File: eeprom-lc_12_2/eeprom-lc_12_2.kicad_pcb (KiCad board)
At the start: 2 copper layers, 97 x 48.3 mm, 13 parts, among them J1 Screw_Terminal_01x03, U1 Controller-RP2040, U2 SN65176BD, U4 EEPROM-RP2040

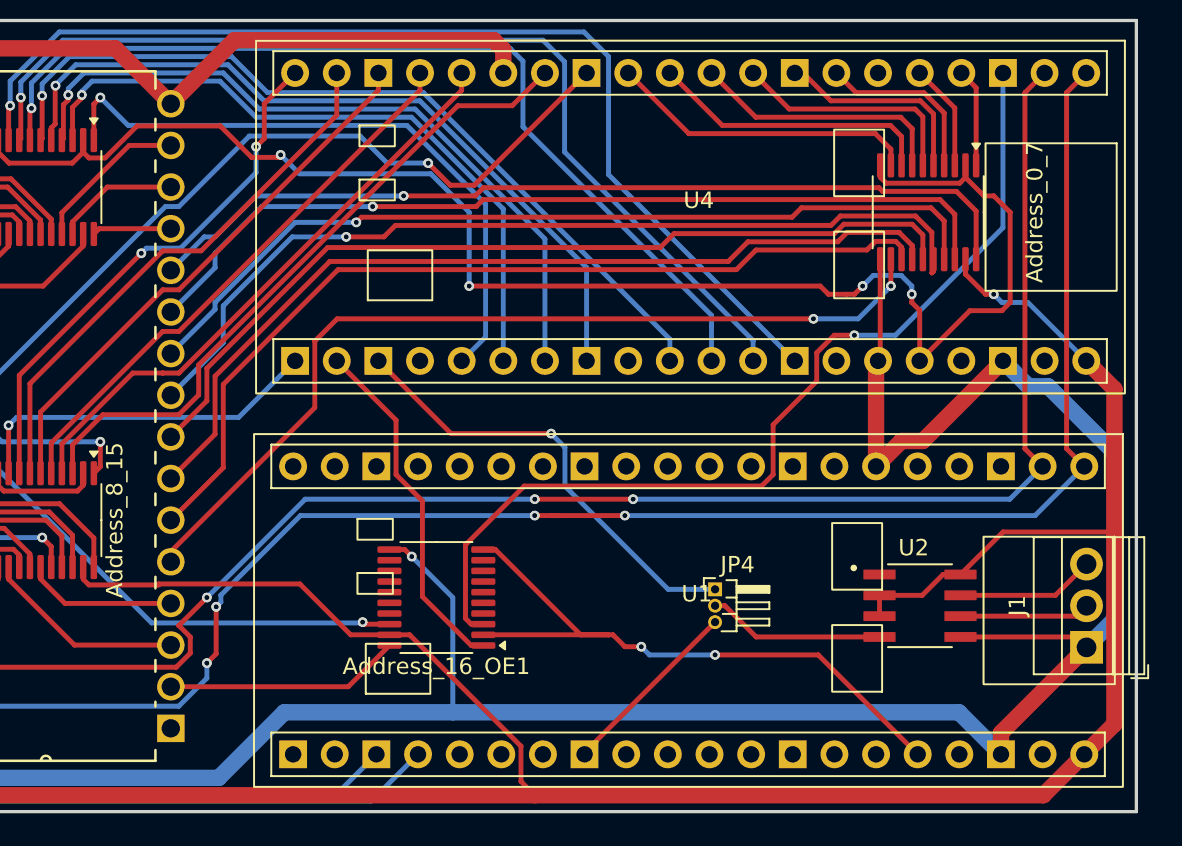
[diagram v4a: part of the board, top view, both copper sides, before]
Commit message: Fix wrong pinheaders
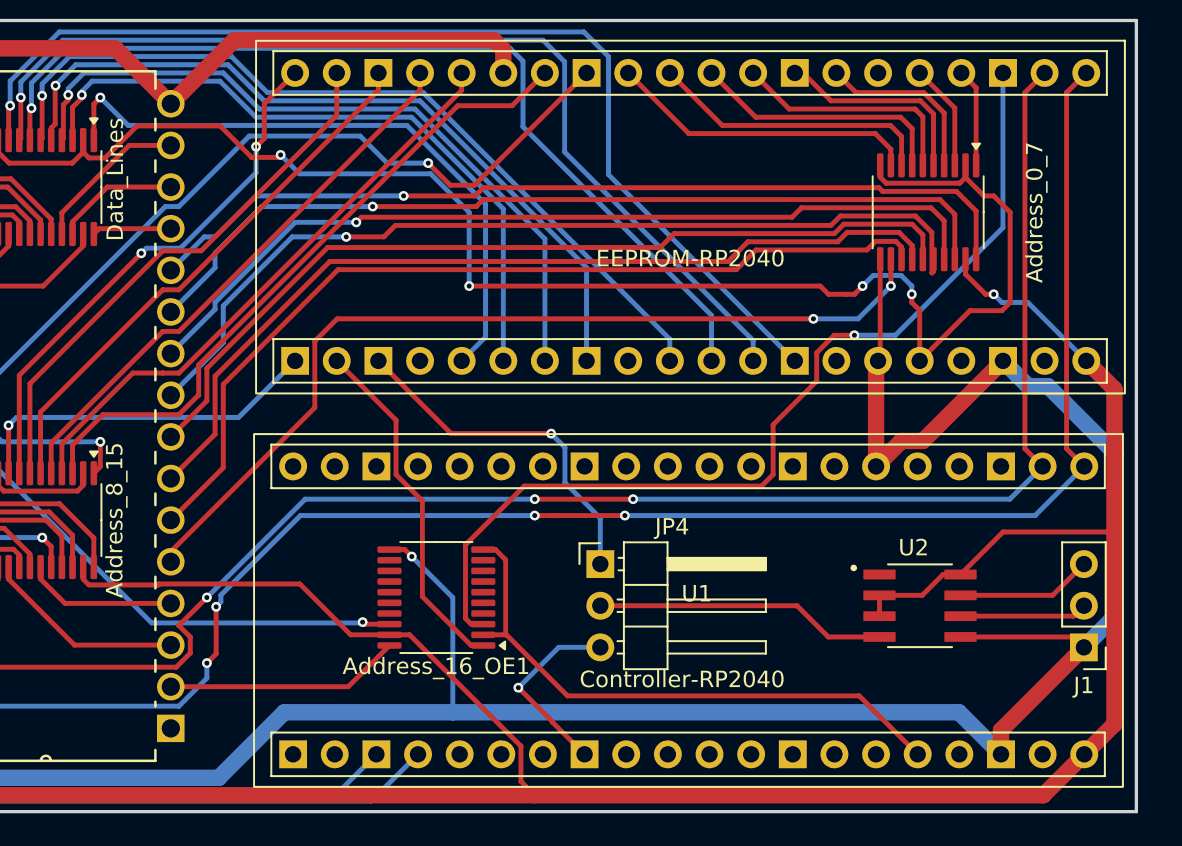
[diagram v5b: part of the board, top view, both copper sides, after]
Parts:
- J1: footprint TerminalBlock:TerminalBlock_Xinya_XY308-2.54-3P_1x03_P2.54mm_Horizontal -> Connector_PinHeader_2.54mm:PinHeader_1x03_P2.54mm_Vertical
- JP4: footprint Connector_PinHeader_1.00mm:PinHeader_1x03_P1.00mm_Horizontal -> Connector_PinHeader_2.54mm:PinHeader_1x03_P2.54mm_Horizontal
- moved JP4 7.17 mm to (140.5, 84.0)
- moved J1 0.16 mm to (170.0, 89.0), turned to 180 degrees
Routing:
- net /DMX_TX: track 10.8 -> 17.8 mm
- net /DMX_TX_EE: track 27.7 -> 21.6 mm
- net /VCC_3V3: track 164.5 -> 160.9 mm, vias 8 -> 6
- net /GND: track 291.3 -> 292.1 mm
- net Net-(J1-Pin_2): track 7.95 -> 8.69 mm
- net /DMX_TX_CON: track 11.4 -> 11.9 mm, vias 0 -> 1
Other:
- board text added: "Data_Lines"

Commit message: Cleanup some traces
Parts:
- UART EE<->ESP: renamed from JP1
- moved JP2 0.85 mm to (88.5, 87.8)
- renumbered JP4 to DMX_TX, U2 to RS-485
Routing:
- net /UART_ESP_RX: track 80.3 -> 65.3 mm
- net /UART_ESP_TX: track 84.2 -> 72.4 mm
- net /UART_EE_RX: track 120.6 -> 119.5 mm, vias 5 -> 3
- net /UART_EE_TX: track 111.2 -> 111.4 mm, vias 3 -> 1
- net /OE_3V3: track 58.8 -> 58.9 mm, vias 1 -> 3
- net /DMX_TX_EE: vias 1 -> 0

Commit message: Finished up the eeprom pcb
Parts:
- removed DMX_TX: DMX_TX, Connector_PinHeader_2.54mm:PinHeader_1x03_P2.54mm_Horizontal
- removed UART EE<->ESP: UART EE <-> ESP 1, TestPoint:TestPoint_2Pads_Pitch2.54mm_Drill0.8mm
- added C1: C_Small, Capacitor_SMD:C_0603_1608Metric_Pad1.08x0.95mm_HandSolder, F.Cu at (170.2, 92.5)
- added C2: C_Small, Capacitor_SMD:C_0603_1608Metric_Pad1.08x0.95mm_HandSolder, F.Cu at (165.5, 84.5)
- added C3: C_Small, Capacitor_SMD:C_0603_1608Metric_Pad1.08x0.95mm_HandSolder, F.Cu at (170.2, 74.8)
- added C4: C_Small, Capacitor_SMD:C_0603_1608Metric_Pad1.08x0.95mm_HandSolder, F.Cu at (96.8, 57.5)
- added C5: C_Small, Capacitor_SMD:C_0603_1608Metric_Pad1.08x0.95mm_HandSolder, F.Cu at (162.0, 67.5)
- added C6: C_Small, Capacitor_SMD:C_0603_1608Metric_Pad1.08x0.95mm_HandSolder, F.Cu at (128.8, 91.8)
- added C7: C_Small, Capacitor_SMD:C_0603_1608Metric_Pad1.08x0.95mm_HandSolder, F.Cu at (108.5, 86.0)
- added C8: C_Small, Capacitor_SMD:C_0603_1608Metric_Pad1.08x0.95mm_HandSolder, F.Cu at (107.5, 65.8)
- added JP1: UART EE <-> ESP 1, TestPoint:TestPoint_2Pads_Pitch2.54mm_Drill0.8mm, F.Cu at (86.0, 87.8)
- added JP4: DMX_TX, Connector_PinHeader_2.54mm:PinHeader_1x03_P2.54mm_Horizontal, F.Cu at (140.5, 84.0)
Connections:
- Address_0_7 pad 10: /VCC_3V3 -> /VCC_3V3_EE
- Address_0_7 pad 2: /VCC_3V3 -> /VCC_3V3_EE
- Address_16_OE1 pad 10: /VCC_3V3 -> /VCC_3V3_CON
- Address_16_OE1 pad 2: /VCC_3V3 -> /VCC_3V3_CON
- Address_8_15 pad 10: /VCC_3V3 -> /VCC_3V3_ESP
- Address_8_15 pad 2: /VCC_3V3 -> /VCC_3V3_ESP
- Data_Lines1 pad 10: /VCC_3V3 -> /VCC_3V3_EE
- Data_Lines1 pad 2: /VCC_3V3 -> /VCC_3V3_EE
- U1 pad 36: /VCC_3V3 -> /VCC_3V3_CON
- U4 pad 36: /VCC_3V3 -> /VCC_3V3_EE
- WIFI-ESP32C6 pad 12: /VCC_3V3 -> /VCC_3V3_ESP
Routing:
- net /VCC_3V3: track 160.9 -> 0.00 mm, vias 6 -> 0
- net /VCC_3V3_EE: track 0.00 -> 94.6 mm, vias 0 -> 4
- net /GND: track 292.1 -> 336.1 mm, vias 3 -> 29
- net /VCC_3V3_CON: track 0.00 -> 35.7 mm
- net /VCC_3V3_ESP: track 0.00 -> 30.9 mm, vias 0 -> 2
- net /VCC_5V: track 214.6 -> 228.3 mm, vias 2 -> 5
- net /A12_5V: track 9.29 -> 11.0 mm
- net /A0_5V: track 54.7 -> 56.4 mm
- net /A8_3V3: track 58.5 -> 57.2 mm
- net /A1_5V: track 54.3 -> 55.5 mm
- net Net-(J1-Pin_2): track 8.69 -> 7.79 mm
- net /A2_5V: track 53.8 -> 54.6 mm
- net /A3_5V: track 56.0 -> 56.6 mm
- added copper zone on B.Cu, net /GND
- added copper zone on F.Cu, net /GND
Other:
- board text added: "2024-05-18"
- board text added: "DMX"
- board text added: "DMX_TX"
- board text added: "MA LC 12/2 Wifi Rev.1"
- board text added: "UART_EE <-> ESP"

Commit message: Last pcb changes before order
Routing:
- net /GND: vias 29 -> 23
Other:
- board text added: "2024-05-22 Jomer.dev"
- board text removed: "2024-05-18"
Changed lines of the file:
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@@
 		)
 	)
-	(gr_text "2024-05-18"
-		(at 81.25 94 0)
+	(gr_text "2024-05-22 Jomer.dev"
+		(at 77.689321 93.98 0)
 		(layer "F.SilkS")
 		(effects
@@
 	(dimension
 		(type aligned)
-		(layer "F.Cu")
+		(layer "Dwgs.User")
 		(pts
 			(xy 76.2 50.8) (xy 114.3 50.8)
 		)
 		(height -5.08)
-		(gr_text "38,1000 mm"
+		(gr_text "38.1000 mm"
 			(at 95.25 43.92 0)
-			(layer "F.Cu")
+			(layer "Dwgs.User")
 			(effects
 				(font
@@
 	)
 	(via
-		(at 100.75 75.75)
-		(size 0.6)
-		(drill 0.3)
-		(layers "F.Cu" "B.Cu")
-		(free yes)
-		(net 18)
-	)
-	(via
 		(at 88 74.5)
 		(size 0.6)
@@
 	)
 	(via
-		(at 130.75 55)
-		(size 0.6)
-		(drill 0.3)
-		(layers "F.Cu" "B.Cu")
-		(free yes)
-		(net 18)
-	)
-	(via
-		(at 112 79.25)
-		(size 0.6)
-		(drill 0.3)
-		(layers "F.Cu" "B.Cu")
-		(free yes)
-		(net 18)
-	)
-	(via
-		(at 104.25 73.75)
-		(size 0.6)
-		(drill 0.3)
-		(layers "F.Cu" "B.Cu")
-		(free yes)
-		(net 18)
-	)
-	(via
 		(at 102.7257 64.8518)
 		(size 0.6)
@@
 	)
 	(via
-		(at 112 82.25)
-		(size 0.6)
-		(drill 0.3)
-		(layers "F.Cu" "B.Cu")
-		(free yes)
-		(net 18)
-	)
-	(via
 		(at 144.25 74.75)
 		(size 0.6)
@@
 	)
 	(via
-		(at 101.75 70)
-		(size 0.6)
-		(drill 0.3)
-		(layers "F.Cu" "B.Cu")
-		(free yes)
-		(net 18)
-	)
-	(via
 		(at 167.5 65)
 		(size 0.6)
@@
 			(thermal_bridge_width 0.5)
 			(island_removal_mode 2)
-			(island_area_min 120)
+			(island_area_min 100)
 		)
 		(polygon
